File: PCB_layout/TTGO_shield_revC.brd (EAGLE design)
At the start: 120.7 x 101.6 mm, 27 parts

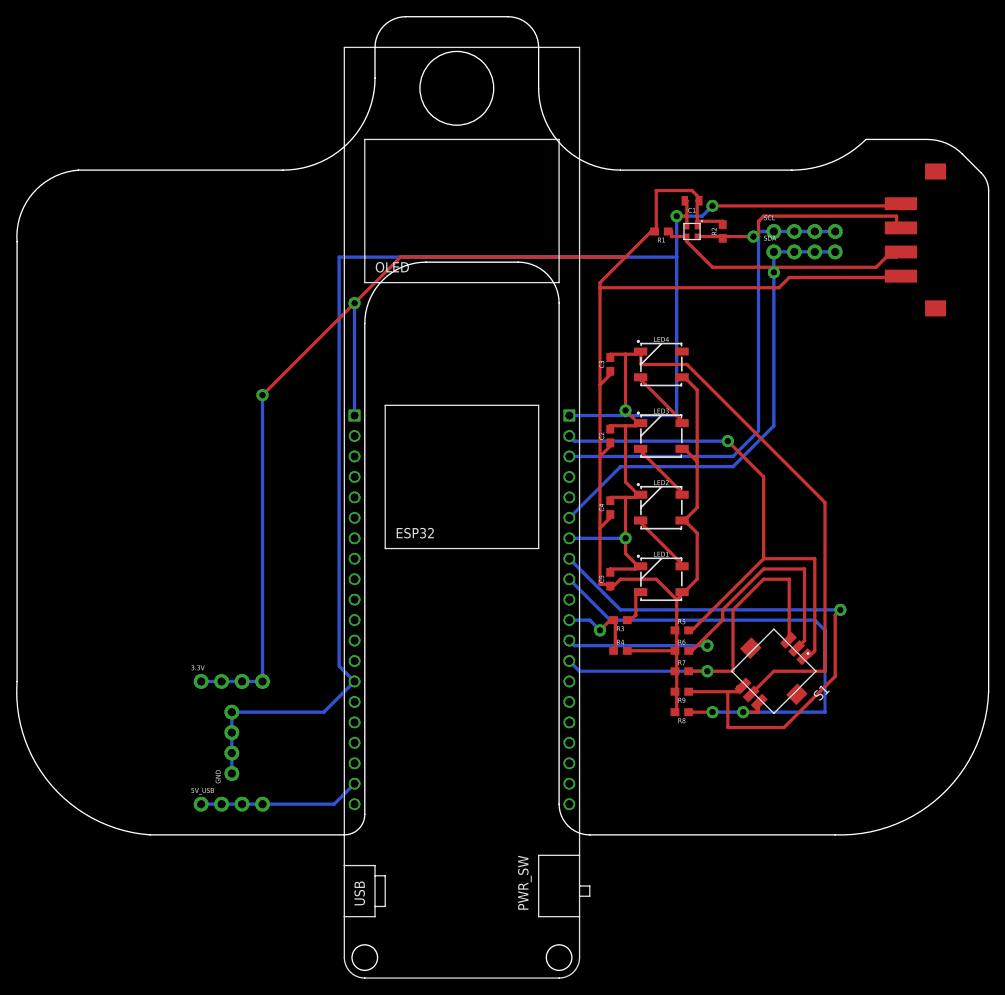
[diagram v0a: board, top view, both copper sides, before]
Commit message: corrected capsense pads
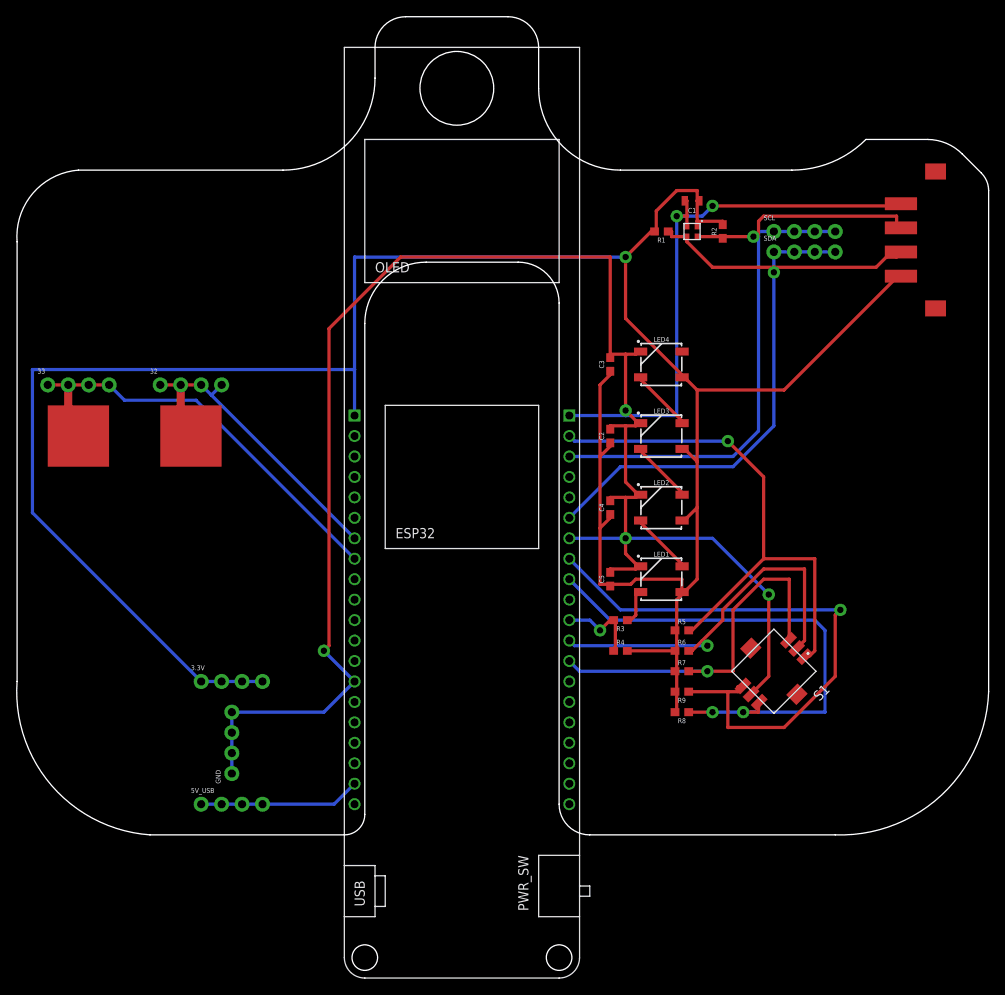
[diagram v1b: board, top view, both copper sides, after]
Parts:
- added 32, 33: (no value), SparkFun-Connectors:1X04_NO_SILK
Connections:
- new net CAP1: 32.1, 32.2, 32.3, 32.4, MAIN.32
- new net CAP2: 33.1, 33.2, 33.3, 33.4, MAIN.33
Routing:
- net CAP2: track 0.00 -> 47.0 mm
- net CAP1: track 0.00 -> 33.8 mm
- net VDD: track 285.7 -> 318.7 mm, vias 2 -> 1
- net GND: track 307.1 -> 279.1 mm, vias 4 -> 6
